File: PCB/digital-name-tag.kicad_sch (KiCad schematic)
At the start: 0 parts

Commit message: did a good chunk of work
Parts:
- added A1: Primordia_Devboard, Module:RaspberryPi_Pico_Common_THT, symbol custom_mcu:Primordia_Devboard
- added J1: Conn_01x04, custom:SSD1306-0.91-OLED-4pin-128x32, symbol Connector_Generic:Conn_01x04
- added SW1, SW2: SW_Push, symbol Switch:SW_Push
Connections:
- new net: A1.13 (GND), A1.18 (GND), A1.23 (GND), A1.28 (GND), A1.3 (GND), A1.38 (GND), A1.8 (GND), A1.D2 (GND)
- new net: A1.4 (GPIO2), SW1.2
- new net: A1.5 (GPIO3), SW2.2
- new net +3.3V: J1.2 (Pin_2)
- new net GND: J1.1 (Pin_1)
- new net SCL: A1.2 (GPIO1), J1.3 (Pin_3)
- new net SDA: A1.1 (GPIO0), J1.4 (Pin_4)

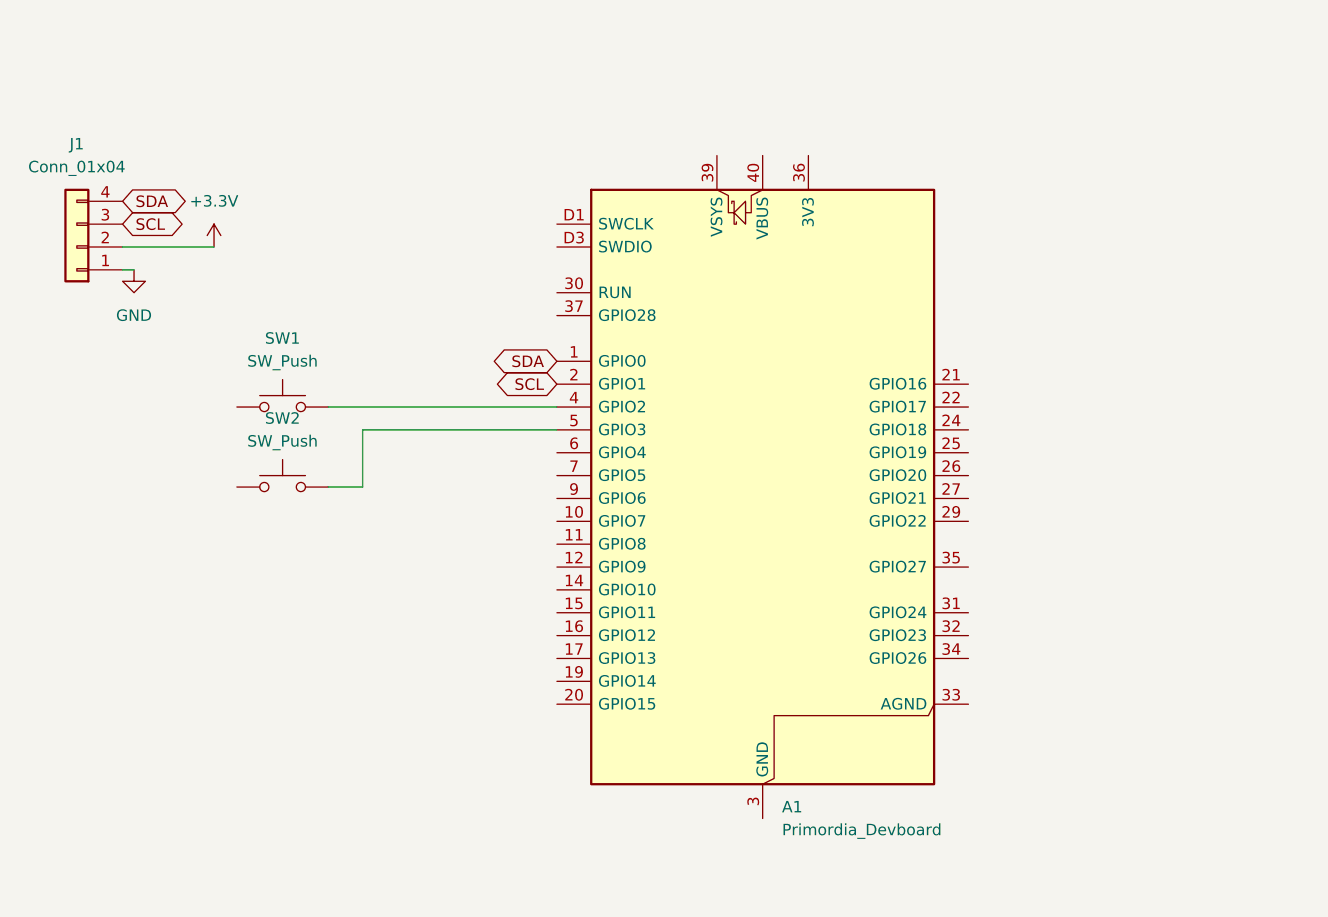
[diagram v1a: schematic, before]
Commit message: layed out the pcb and added silkscreen art
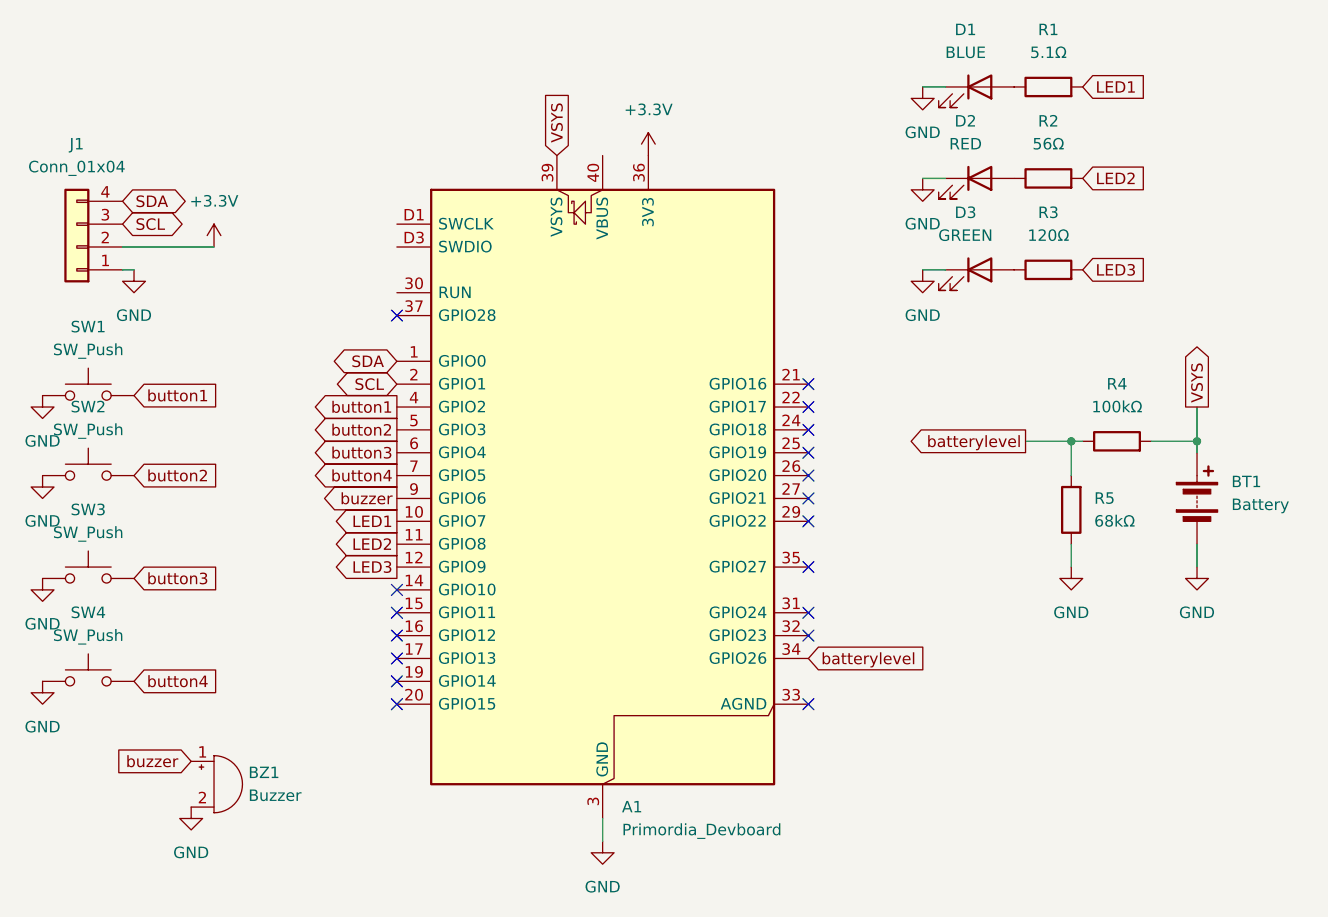
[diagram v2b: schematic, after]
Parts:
- added BT1: Battery, Battery:BatteryHolder_TruPower_BH-331P_3xAA, symbol Device:Battery
- added BZ1: Buzzer, Buzzer_Beeper:Buzzer_D14mm_H7mm_P10mm, symbol Device:Buzzer
- added D1: BLUE, LED_THT:LED_D5.0mm, symbol Device:LED
- added D2: RED, LED_THT:LED_D3.0mm, symbol Device:LED
- added D3: GREEN, LED_THT:LED_D5.0mm, symbol Device:LED
- added R1: 5.1Ω, Resistor_THT:R_Axial_DIN0414_L11.9mm_D4.5mm_P5.08mm_Vertical, symbol Device:R
- added R2: 56Ω, Resistor_THT:R_Axial_DIN0516_L15.5mm_D5.0mm_P20.32mm_Horizontal, symbol Device:R
- added R3: 120Ω, Resistor_THT:R_Axial_DIN0411_L9.9mm_D3.6mm_P12.70mm_Horizontal, symbol Device:R
- added R4: 100kΩ, Resistor_THT:R_Axial_DIN0204_L3.6mm_D1.6mm_P7.62mm_Horizontal, symbol Device:R
- added R5: 68kΩ, Resistor_THT:R_Axial_DIN0207_L6.3mm_D2.5mm_P2.54mm_Vertical, symbol Device:R
- added SW3, SW4: SW_Push, Button_Switch_THT:SW_PUSH_6mm, symbol Switch:SW_Push
- SW1, SW2: footprint (none) -> Button_Switch_THT:SW_PUSH_6mm
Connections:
- net +3.3V: now also A1.36 (3V3)
- net GND: now also A1.13 (GND), A1.18 (GND), A1.23 (GND), A1.28 (GND), A1.3 (GND), A1.38 (GND), A1.8 (GND), A1.D2 (GND), SW1.1, SW2.1, BT1.2 (-), BZ1.2 (-), D1.1 (K), D2.1 (K), D3.1 (K), R5.1, SW3.1, SW4.1
- net LED1: now reaches A1.10 (GPIO7)
- net LED1: now also R1.2
- net LED2: now reaches A1.11 (GPIO8)
- net LED2: now also R2.2
- net LED3: now reaches A1.12 (GPIO9)
- net LED3: now also R3.2
- net batterylevel: now reaches A1.34 (GPIO26)
- net batterylevel: now also R4.1, R5.2
- net VSYS: now reaches A1.39 (VSYS)
- net VSYS: now also BT1.1 (+), R4.2
- net button1: now reaches A1.4 (GPIO2), SW1.2
- net button2: now reaches A1.5 (GPIO3), SW2.2
- net button3: now reaches A1.6 (GPIO4)
- net button3: now also SW3.2
- net button4: now reaches A1.7 (GPIO5)
- net button4: now also SW4.2
- net buzzer: now reaches A1.9 (GPIO6)
- net buzzer: now also BZ1.1 (+)
- new net: D2.2 (A), R2.1
- new net: D1.2 (A), R1.1
- new net: D3.2 (A), R3.1
- no-connect marks 0 -> 18
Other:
- moved on the sheet: A1, SW1, SW2
